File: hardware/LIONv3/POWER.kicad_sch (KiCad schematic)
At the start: 28 parts, among them U10 INA226AIDGSR, U11 TPS259474ARPWR, U12 XL-1608UGC-04, U13 XL-1608SURC-06, U16 HC-1_25-2PWT, U17 HC-1_25-2PWT, U18 HC-1_25-2PWT, U20 TLV76733DRVR

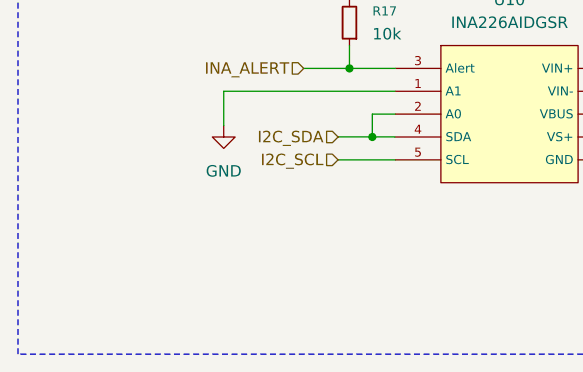
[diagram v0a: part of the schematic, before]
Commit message: feat(hardware): annotate schematic with I2C addresses
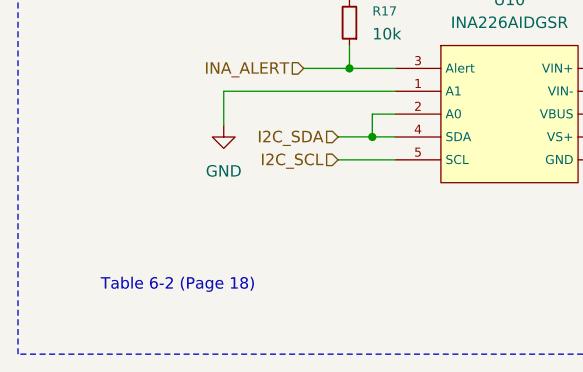
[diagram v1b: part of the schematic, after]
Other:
- note added: "Table 6-2 (Page 18)"
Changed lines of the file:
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@@
+		)
+	)
+	(text "Table 6-2 (Page 18)"
+		(exclude_from_sim no)
+		(at 31.75 124.46 0)
+		(effects
+			(font
+				(size 1.27 1.27)
+			)
 		)
 	)
@@
 		)
 	)
+	(table
+		(column_count 5)
+		(border
+			(external no)
+			(header yes)
+			(stroke
+				(width 0)
+				(type solid)
+			)
+		)
+		(separators
+			(rows no)
+			(cols no)
+		)
+		(column_widths 5.08 5.08 10.16 6.35 5.08)
+		(row_heights 2.54 2.54)
+		(cells
+			(table_cell "A0"
+				(exclude_from_sim no)
+				(at 15.24 125.73 0)
+				(size 5.08 2.54)
+				(margins 0.9525 0.9525 0.9525 0.9525)
+				(span 1 1)
+				(fill
+					(type none)
+				)
+				(effects
+					(font
+						(size 1.27 1.27)
+					)
+					(justify left top)
+				)
+			)
+			(table_cell "A1"
+				(exclude_from_sim no)
+				(at 20.32 125.73 0)
+				(size 5.08 2.54)
+				(margins 0.9525 0.9525 0.9525 0.9525)
+				(span 1 1)
+				(fill
+					(type none)
+				)
+				(effects
+					(font
+						(size 1.27 1.27)
+					)
+					(justify left top)
+				)
+			)
+			(table_cell "Binary"
+				(exclude_from_sim no)
+				(at 25.4 125.73 0)
+				(size 10.16 2.54)
+				(margins 0.9525 0.9525 0.9525 0.9525)
+				(span 1 1)
+				(fill
+					(type none)
+				)
+				(effects
+					(font
+						(size 1.27 1.27)
+					)
+					(justify left top)
+				)
+			)
+			(table_cell "Hex"
+				(exclude_from_sim no)
+				(at 35.56 125.73 0)
+				(size 6.35 2.54)
+				(margins 0.9525 0.9525 0.9525 0.9525)
+				(span 1 1)
+				(fill
+					(type none)
+				)
+				(effects
+					(font
+						(size 1.27 1.27)
+					)
+					(justify left top)
+				)
+			)
+			(table_cell "Dec"
+				(exclude_from_sim no)
+				(at 41.91 125.73 0)
+				(size 5.08 2.54)
+				(margins 0.9525 0.9525 0.9525 0.9525)
+				(span 1 1)
+				(fill
+					(type none)
+				)
+				(effects
+					(font
+						(size 1.27 1.27)
+					)
+					(justify left top)
+				)
+			)
+			(table_cell "SDA"
+				(exclude_from_sim no)
+				(at 15.24 128.27 0)
+				(size 5.08 2.54)
+				(margins 0.9525 0.9525 0.9525 0.9525)
+				(span 1 1)
+				(fill
+					(type none)
+				)
+				(effects
+					(font
+						(size 1.27 1.27)
+					)
+					(justify left top)
+				)
+			)
+			(table_cell "GND"
+				(exclude_from_sim no)
+				(at 20.32 128.27 0)
+				(size 5.08 2.54)
+				(margins 0.9525 0.9525 0.9525 0.9525)
+				(span 1 1)
+				(fill
+					(type none)
+				)
+				(effects
+					(font
+						(size 1.27 1.27)
+					)
+					(justify left top)
+				)
+			)
+			(table_cell "1000010"
+				(exclude_from_sim no)
+				(at 25.4 128.27 0)
+				(size 10.16 2.54)
+				(margins 0.9525 0.9525 0.9525 0.9525)
+				(span 1 1)
+				(fill
+					(type none)
+				)
+				(effects
+					(font
+						(size 1.27 1.27)
+					)
+					(justify left top)
+				)
+			)
+			(table_cell "0x42"
+				(exclude_from_sim no)
+				(at 35.56 128.27 0)
+				(size 6.35 2.54)
+				(margins 0.9525 0.9525 0.9525 0.9525)
+				(span 1 1)
+				(fill
+					(type none)
+				)
+				(effects
+					(font
+						(size 1.27 1.27)
+					)
+					(justify left top)
+				)
+			)
+			(table_cell "66"
+				(exclude_from_sim no)
+				(at 41.91 128.27 0)
+				(size 5.08 2.54)
+				(margins 0.9525 0.9525 0.9525 0.9525)
+				(span 1 1)
+				(fill
+					(type none)
+				)
+				(effects
+					(font
+						(size 1.27 1.27)
+					)
+					(justify left top)
+				)
+			)
+		)
+	)

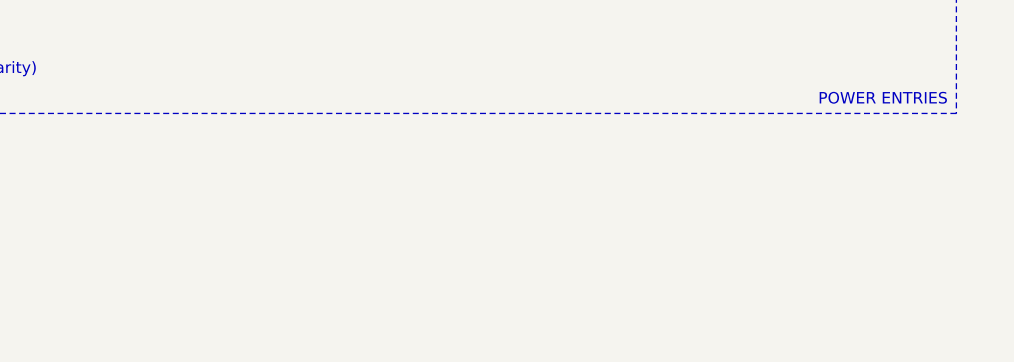
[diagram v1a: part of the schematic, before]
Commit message: refactor(hardware): reorganize schematic
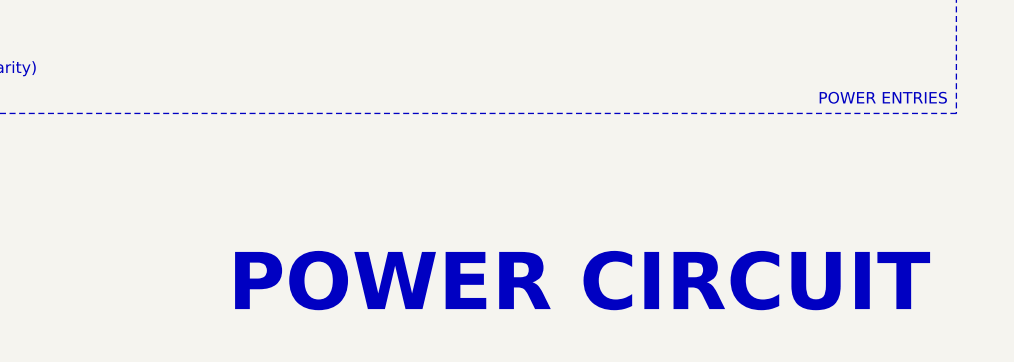
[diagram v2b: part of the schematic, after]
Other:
- note added: "POWER CIRCUIT"
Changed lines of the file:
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@@
 		(comment 3 "2026-08-12")
+	)
+	(text "POWER CIRCUIT"
+		(exclude_from_sim no)
+		(at 241.3 151.13 0)
+		(effects
+			(font
+				(size 6.35 6.35)
+				(thickness 1.27)
+				(bold yes)
+			)
+		)
 	)
 	(text "3.3V@800mA"

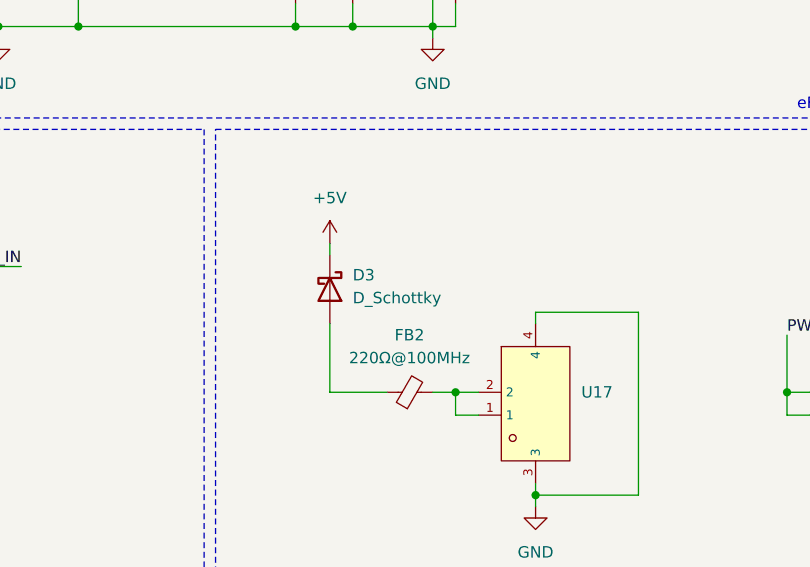
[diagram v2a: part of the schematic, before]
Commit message: refactor(hardware): add MPN diodes and ferrite beads
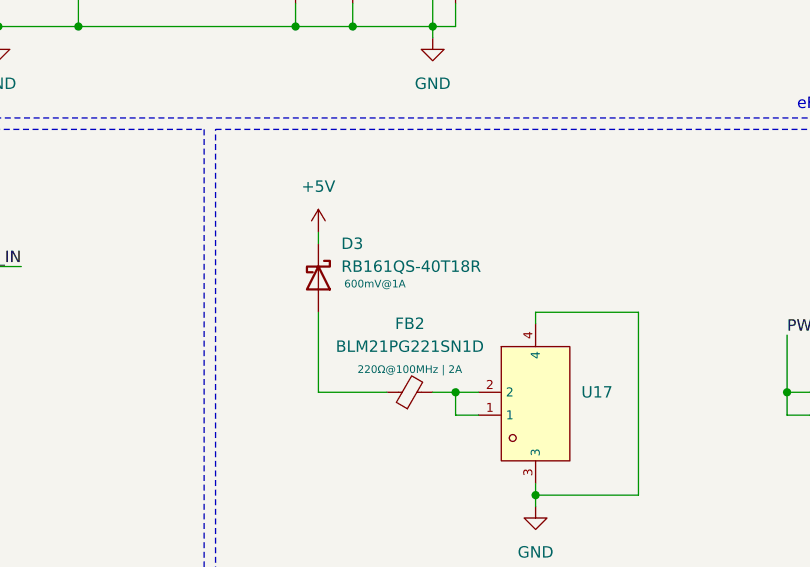
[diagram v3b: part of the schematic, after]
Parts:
- D3: value D_Schottky -> RB161QS-40T18R; Rating (none) -> 600mV@1A
- FB2: value 220Ω@100MHz -> BLM21PG221SN1D; Rating (none) -> 220Ω@100MHz | 2A
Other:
- moved on the sheet: D3
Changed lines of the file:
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@@
 	(wire
 		(pts
-			(xy 153.67 92.71) (xy 153.67 100.33)
+			(xy 152.4 91.44) (xy 152.4 100.33)
 		)
 		(stroke
@@
 	(wire
 		(pts
-			(xy 153.67 83.82) (xy 153.67 85.09)
+			(xy 152.4 82.55) (xy 152.4 83.82)
 		)
 		(stroke
@@
 	(wire
 		(pts
-			(xy 153.67 100.33) (xy 160.02 100.33)
+			(xy 152.4 100.33) (xy 160.02 100.33)
 		)
 		(stroke
@@
 	(symbol
 		(lib_id "power:+5V")
-		(at 153.67 83.82 0)
+		(at 152.4 82.55 0)
 		(unit 1)
 		(body_style 1)
@@
 		(fields_autoplaced yes)
 		(property "Reference" "#PWR016"
-			(at 153.67 87.63 0)
+			(at 152.4 86.36 0)
 			(hide yes)
 			(show_name no)
@@
 		)
 		(property "Value" "+5V"
-			(at 153.67 78.74 0)
+			(at 152.4 77.47 0)
 			(show_name no)
 			(do_not_autoplace no)
@@
 		)
 		(property "Footprint" ""
-			(at 153.67 83.82 0)
+			(at 152.4 82.55 0)
 			(hide yes)
 			(show_name no)
@@
 		)
 		(property "Datasheet" ""
-			(at 153.67 83.82 0)
+			(at 152.4 82.55 0)
 			(hide yes)
 			(show_name no)
@@
 		)
 		(property "Description" "Power symbol creates a global label with name \"+5V\""
-			(at 153.67 83.82 0)
+			(at 152.4 82.55 0)
 			(hide yes)
 			(show_name no)
@@
 		(in_pos_files yes)
 		(dnp no)
-		(fields_autoplaced yes)
 		(property "Reference" "FB2"
-			(at 162.5219 93.98 90)
-			(show_name no)
-			(do_not_autoplace no)
-			(effects
-				(font
-					(size 1.27 1.27)
-				)
-			)
-		)
-		(property "Value" "220Ω@100MHz"
-			(at 162.5219 96.52 90)
+			(at 162.56 92.71 90)
+			(show_name no)
+			(do_not_autoplace no)
+			(effects
+				(font
+					(size 1.27 1.27)
+				)
+			)
+		)
+		(property "Value" "BLM21PG221SN1D"
+			(at 162.56 95.25 90)
 			(show_name no)
 			(do_not_autoplace no)
@@
 				(font
 					(size 1.27 1.27)
+				)
+			)
+		)
+		(property "Rating" "220Ω@100MHz | 2A"
+			(at 162.56 97.79 90)
+			(show_name no)
+			(do_not_autoplace no)
+			(effects
+				(font
+					(size 0.8467 0.8467)
 				)
 			)
@@
 	(symbol
 		(lib_id "Device:D_Schottky")
-		(at 153.67 88.9 270)
+		(at 152.4 87.63 270)
 		(unit 1)
 		(body_style 1)
@@
 		(in_pos_files yes)
 		(dnp no)
-		(fields_autoplaced yes)
 		(property "Reference" "D3"
-			(at 156.21 87.3124 90)
+			(at 154.94 83.82 90)
 			(show_name no)
 			(do_not_autoplace no)
@@
 			)
 		)
-		(property "Value" "D_Schottky"
-			(at 156.21 89.8524 90)
+		(property "Value" "RB161QS-40T18R"
+			(at 154.94 86.36 90)
 			(show_name no)
 			(do_not_autoplace no)
@@
 		)
 		(property "Footprint" "LIONv3-Footprints:X2-DFN1006-2_L1.0-W0.6-P0.65-RD"
-			(at 153.67 88.9 0)
-			(hide yes)
-			(show_name no)
-			(do_not_autoplace no)
-			(effects
-				(font
-					(size 1.27 1.27)
-				)
-			)
-		)
-		(property "Datasheet" ""
-			(at 153.67 88.9 0)
+			(at 152.4 87.63 0)
+			(hide yes)
+			(show_name no)
+			(do_not_autoplace no)
+			(effects
+				(font
+					(size 1.27 1.27)
+				)
+			)
+		)
+		(property "Datasheet" "https://www.lcsc.com/datasheet/C2837790.pdf"
+			(at 152.4 87.63 0)
 			(hide yes)
 			(show_name no)
@@
 		)
 		(property "Description" "Schottky diode"
-			(at 153.67 88.9 0)
+			(at 152.4 87.63 0)
 			(hide yes)
 			(show_name no)
@@
 		)
 		(property "LCSC" "C2837790"
-			(at 153.67 88.9 0)
-			(hide yes)
-			(show_name no)
-			(do_not_autoplace no)
-			(effects
-				(font
-					(size 1.27 1.27)
-				)
-			)
+			(at 152.4 87.63 0)
+			(hide yes)
+			(show_name no)
+			(do_not_autoplace no)
+			(effects
+				(font
+					(size 1.27 1.27)
+				)
+			)
+		)
+		(property "Rating" "600mV@1A"
+			(at 158.6828 88.2846 90)
+			(show_name no)
+			(do_not_autoplace no)
+			(effects
+				(font
+					(size 0.8467 0.8467)
+				)
+			)

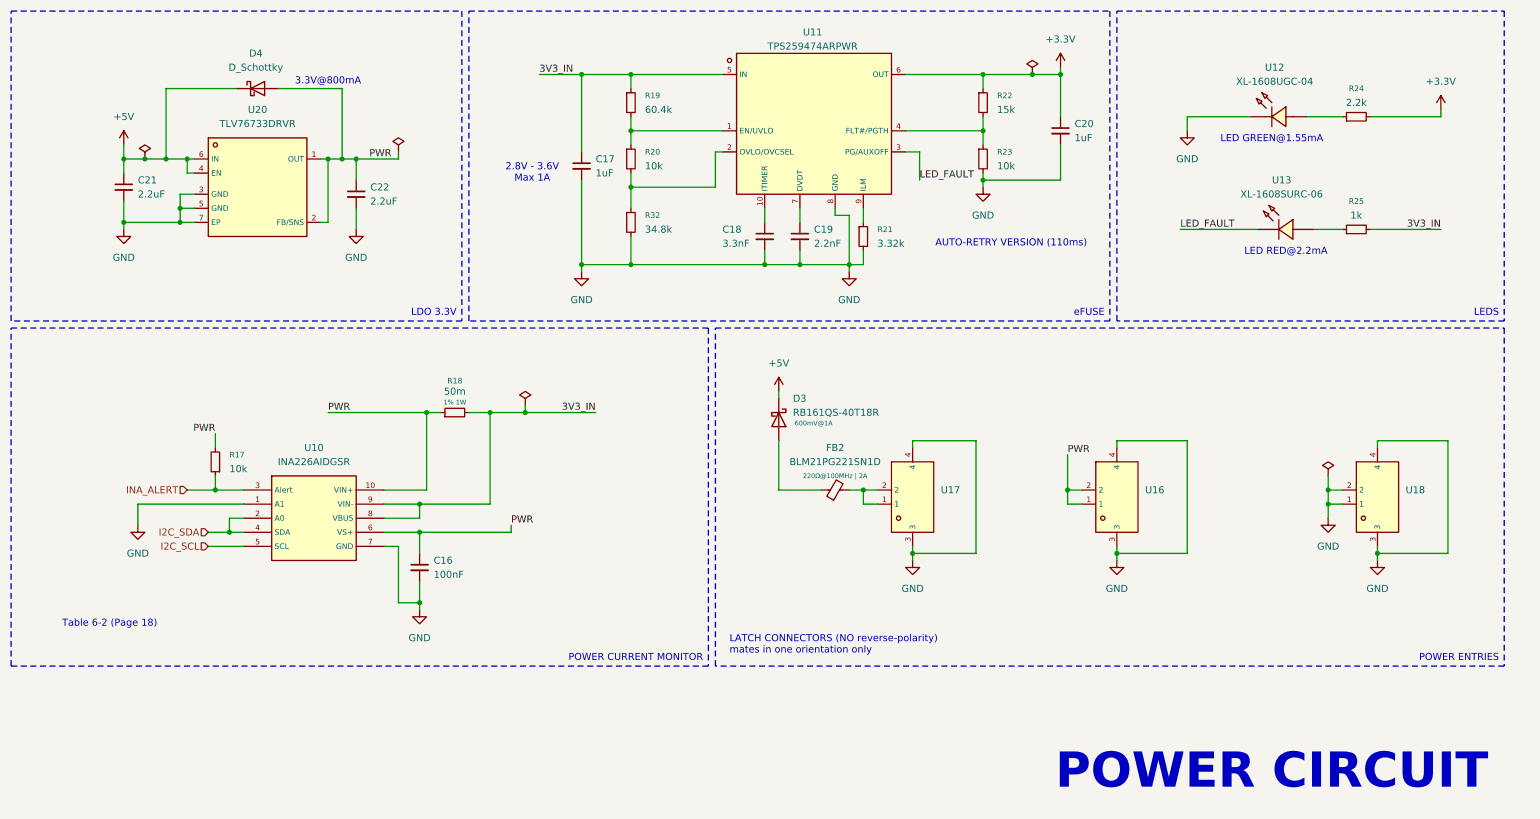
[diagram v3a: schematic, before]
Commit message: refactor(hardware): rename power symbols
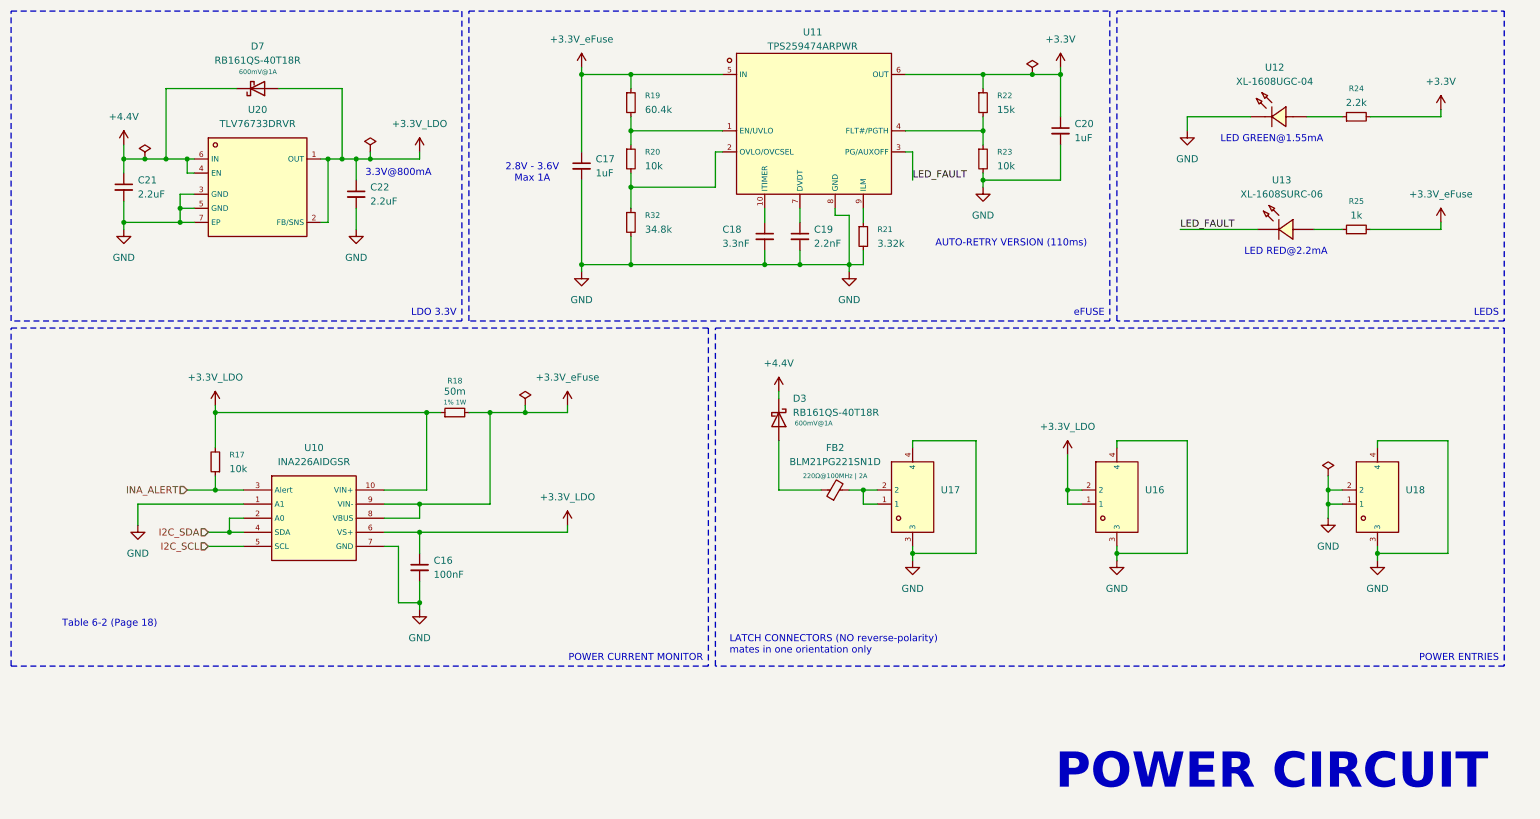
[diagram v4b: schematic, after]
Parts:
- removed D4: D_Schottky, LIONv3-Footprints:X2-DFN1006-2_L1.0-W0.6-P0.65-RD, symbol Device:D_Schottky
- added D7: RB161QS-40T18R, LIONv3-Footprints:X2-DFN1006-2_L1.0-W0.6-P0.65-RD, symbol Device:D_Schottky
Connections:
- net +5V renamed +4.4V
- net +4.4V: now also D7.1 (K)
- net 3V3_IN renamed +3.3V_eFuse
- net PWR renamed +3.3V_LDO
- net +3.3V_LDO: now also D7.2 (A)

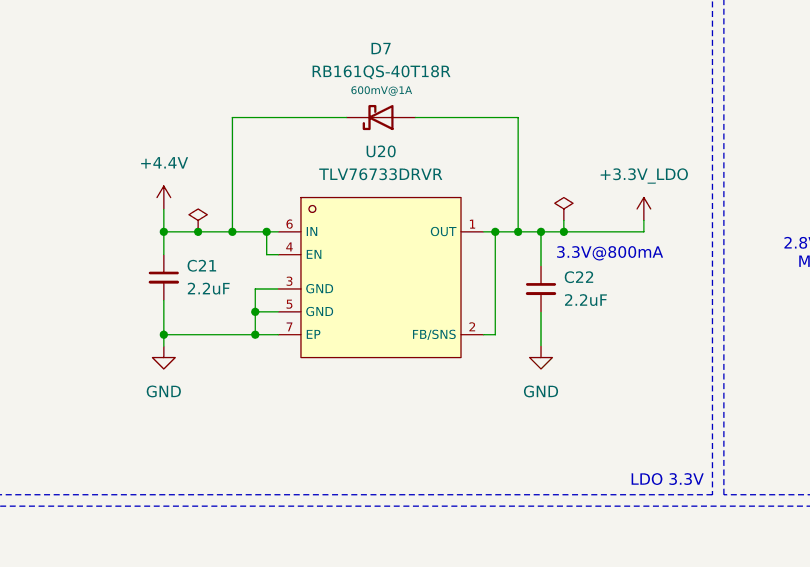
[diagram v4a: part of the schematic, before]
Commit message: feat(hardware): change LDO capacitors from 2.2uF to 22uF
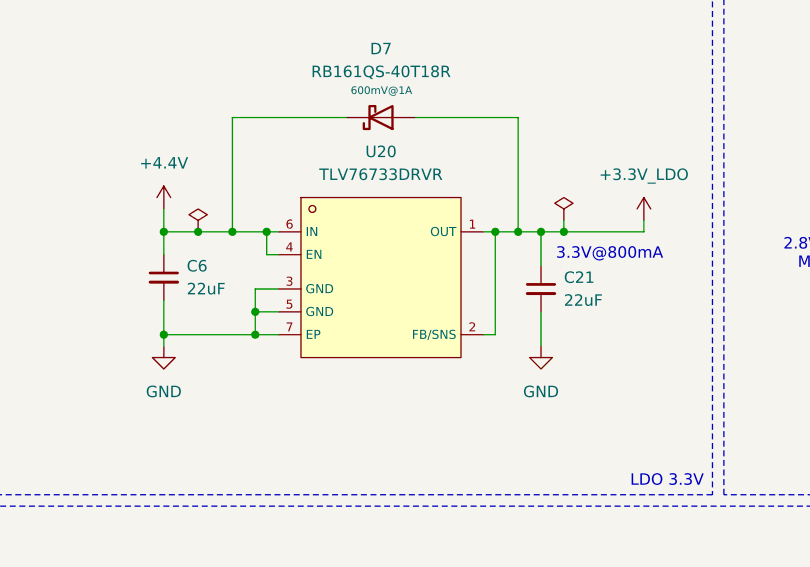
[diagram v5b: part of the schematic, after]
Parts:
- removed C22: 2.2uF, Capacitor_SMD:C_0603_1608Metric, symbol Device:C_Small
- added C6: 22uF, Capacitor_SMD:C_0805_2012Metric, symbol Device:C_Small
- C21: value 2.2uF -> 22uF; footprint Capacitor_SMD:C_0603_1608Metric -> Capacitor_SMD:C_0805_2012Metric; LCSC C913904 -> C45783
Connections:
- net +3.3V_LDO: now also C21.1
- net +4.4V: now also C6.1; no longer C21.1
- net GND: now also C6.2

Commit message: feat(hardware): major schematic improvements
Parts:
- R24: value 2.2k -> 120
- R25: value 1k -> 430
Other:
- note added: "(3.3-2)/430"
- note added: "(3.3-3)/120"
- note added: "LED GREEN@3mA"
- note added: "LED RED@3mA"
- note removed: "LED GREEN@1.55mA"
- note removed: "LED RED@2.2mA"
- moved on the sheet: C16, D3, FB2, R17, R18, U10, U16, U17, U18
